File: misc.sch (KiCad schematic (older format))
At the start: 39 parts, among them J13 MICROSD_SLOT_TFP09-2-12B, P13 EXT_SD, P14 LCD, P15 LIMIT_SWITCHES, P16 LIMIT_SWITCHES_V, P17 CONN_01X03, P18 CONN_01X03, P19 CONN_01X03, P20 CONN_01X03, P21 THERMISTORS, P25 I2C, SW1 RESET, U3 ESP-12E

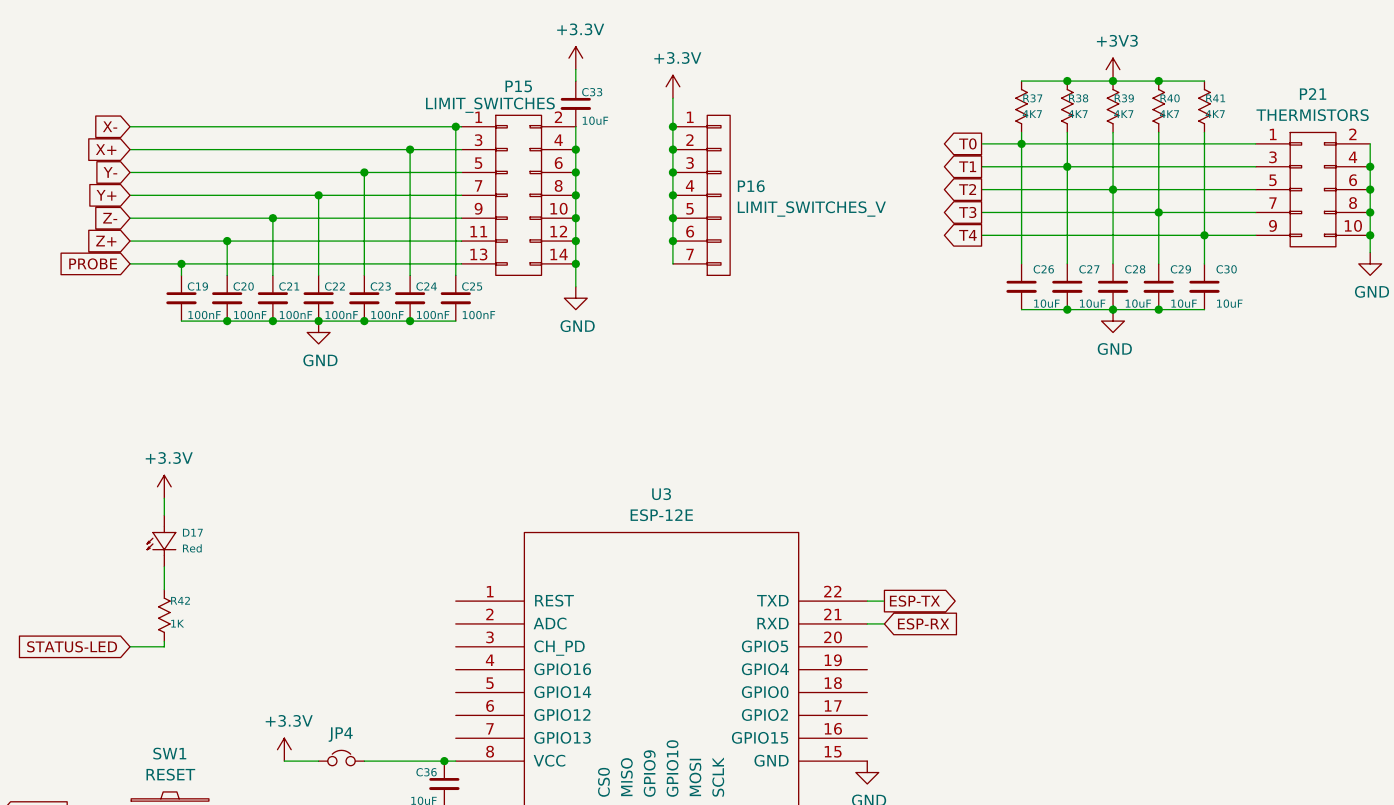
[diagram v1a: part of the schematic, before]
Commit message: Added component specifications
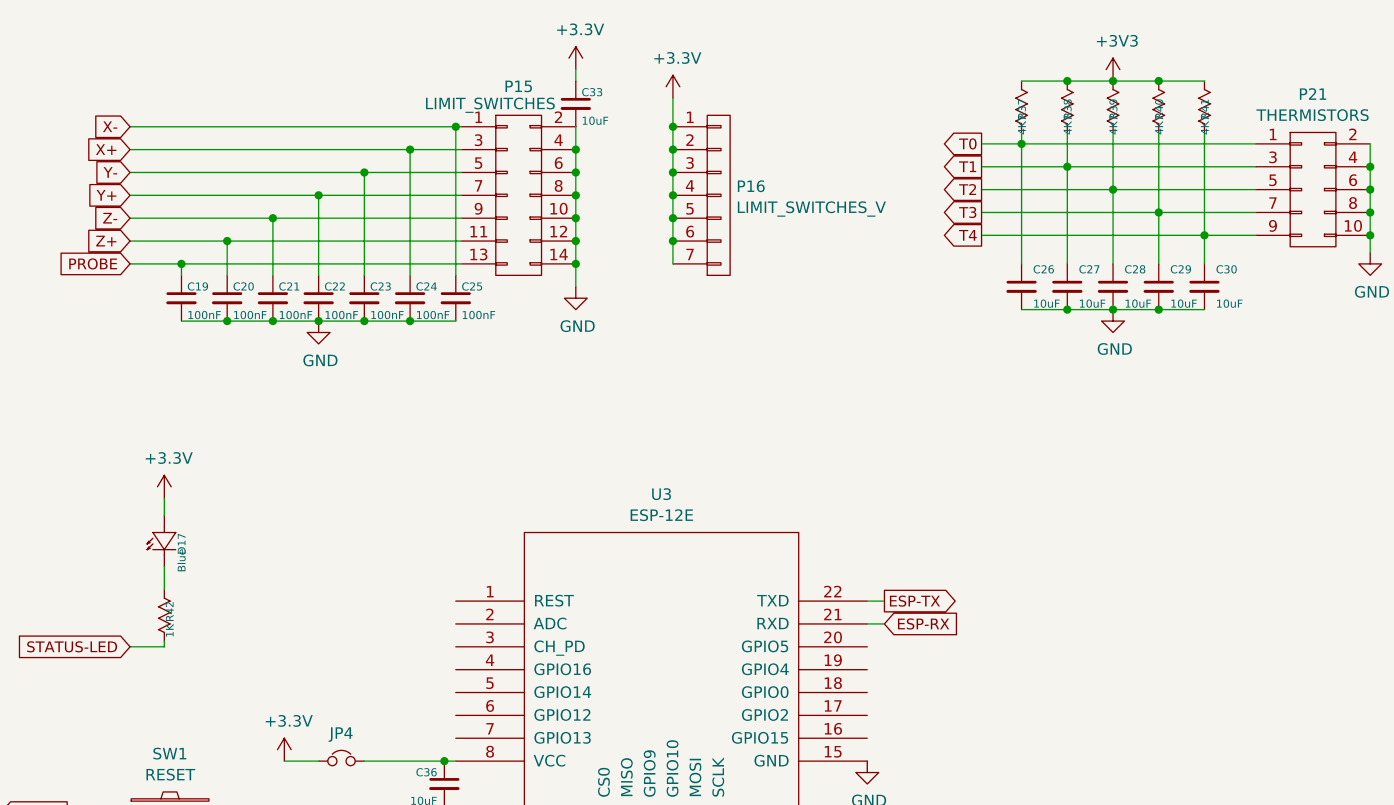
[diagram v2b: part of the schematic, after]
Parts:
- C18, C26, C27, C28, C29, C30, C33, C34, C36: Specification (none) -> X7R/X5R; VoltageRating (none) -> 6.3V
- C19, C20, C21, C22, C23, C24, C25, C31: Specification (none) -> X7R; VoltageRating (none) -> 16V
- D17: value Red -> Blue
- J13: ManufacturerNo (none) -> TFP09-2-12B
- R37, R38, R39, R40, R41: Specification (none) -> 1%
- R42: Specification (none) -> 5%
- U3: Manufacturer (none) -> AI-Thinker; ManufacturerNo (none) -> ESP-12E
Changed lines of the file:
@@
 F 2 "geda-footprints:MICROSD_SLOT_TFP09-2-12B" H 2075 2350 60  0001 C CNN
 F 3 "" H 2075 2350 60  0000 C CNN
+F 4 "TFP09-2-12B" H 2075 2350 135 0001 L CNN "ManufacturerNo"
 	1    2075 2350
 	1    0    0    -1
@@
 F 2 "capacitors:C_0805" H 1825 1875 50  0001 C CNN
 F 3 "" H 1825 1875 50  0000 C CNN
+F 4 "6.3V" H 1825 1875 135 0001 L CNN "VoltageRating"
+F 5 "X7R/X5R" H 1825 1875 135 0001 L CNN "Specification"
 	1    1825 1875
 	1    0    0    -1
@@
 U 1 1 568D8616
 P 8750 1325
-F 0 "R39" V 8827 1403 34  0000 L CNN
-F 1 "4K7" V 8896 1403 34  0000 L CNN
+F 0 "R39" H 8827 1403 34  0000 L CNN
+F 1 "4K7" H 8896 1403 34  0000 L CNN
 F 2 "resistors:R_0603" H 8750 1325 60  0001 C CNN
 F 3 "" H 8750 1325 60  0000 C CNN
+F 4 "1%" H 8750 1325 135 0001 L CNN "Specification"
 	1    8750 1325
 	0    1    1    0
@@
 F 2 "capacitors:C_0805" H 9225 2225 50  0001 C CNN
 F 3 "" H 9225 2225 50  0000 C CNN
+F 4 "6.3V" H 9225 2225 135 0001 L CNN "VoltageRating"
+F 5 "X7R/X5R" H 9225 2225 135 0001 L CNN "Specification"
 	1    9225 2225
 	1    0    0    -1
@@
 U 1 1 568D8A52
 P 9150 1325
-F 0 "R41" V 9227 1403 34  0000 L CNN
-F 1 "4K7" V 9296 1403 34  0000 L CNN
+F 0 "R41" H 9227 1403 34  0000 L CNN
+F 1 "4K7" H 9296 1403 34  0000 L CNN
 F 2 "resistors:R_0603" H 9150 1325 60  0001 C CNN
 F 3 "" H 9150 1325 60  0000 C CNN
+F 4 "1%" H 9150 1325 135 0001 L CNN "Specification"
 	1    9150 1325
 	0    1    1    0
@@
 U 1 1 568D8AA1
 P 8950 1325
-F 0 "R40" V 9027 1403 34  0000 L CNN
-F 1 "4K7" V 9096 1403 34  0000 L CNN
+F 0 "R40" H 9027 1403 34  0000 L CNN
+F 1 "4K7" H 9096 1403 34  0000 L CNN
 F 2 "resistors:R_0603" H 8950 1325 60  0001 C CNN
 F 3 "" H 8950 1325 60  0000 C CNN
+F 4 "1%" H 8950 1325 135 0001 L CNN "Specification"
 	1    8950 1325
 	0    1    1    0
@@
 U 1 1 568D8B17
 P 8550 1325
-F 0 "R38" V 8627 1403 34  0000 L CNN
-F 1 "4K7" V 8696 1403 34  0000 L CNN
+F 0 "R38" H 8627 1403 34  0000 L CNN
+F 1 "4K7" H 8696 1403 34  0000 L CNN
 F 2 "resistors:R_0603" H 8550 1325 60  0001 C CNN
 F 3 "" H 8550 1325 60  0000 C CNN
+F 4 "1%" H 8550 1325 135 0001 L CNN "Specification"
 	1    8550 1325
 	0    1    1    0
@@
 U 1 1 568D8BC2
 P 8350 1325
-F 0 "R37" V 8427 1403 34  0000 L CNN
-F 1 "4K7" V 8496 1403 34  0000 L CNN
+F 0 "R37" H 8427 1403 34  0000 L CNN
+F 1 "4K7" H 8496 1403 34  0000 L CNN
 F 2 "resistors:R_0603" H 8350 1325 60  0001 C CNN
 F 3 "" H 8350 1325 60  0000 C CNN
+F 4 "1%" H 8350 1325 135 0001 L CNN "Specification"
 	1    8350 1325
 	0    1    1    0
@@
 F 2 "capacitors:C_0805" H 9025 2225 50  0001 C CNN
 F 3 "" H 9025 2225 50  0000 C CNN
+F 4 "6.3V" H 9025 2225 135 0001 L CNN "VoltageRating"
+F 5 "X7R/X5R" H 9025 2225 135 0001 L CNN "Specification"
 	1    9025 2225
 	1    0    0    -1
@@
 F 2 "capacitors:C_0805" H 8825 2225 50  0001 C CNN
 F 3 "" H 8825 2225 50  0000 C CNN
+F 4 "6.3V" H 8825 2225 135 0001 L CNN "VoltageRating"
+F 5 "X7R/X5R" H 8825 2225 135 0001 L CNN "Specification"
 	1    8825 2225
 	1    0    0    -1
@@
 F 2 "capacitors:C_0805" H 8625 2225 50  0001 C CNN
 F 3 "" H 8625 2225 50  0000 C CNN
+F 4 "6.3V" H 8625 2225 135 0001 L CNN "VoltageRating"
+F 5 "X7R/X5R" H 8625 2225 135 0001 L CNN "Specification"
 	1    8625 2225
 	1    0    0    -1
@@
 F 2 "capacitors:C_0805" H 8425 2225 50  0001 C CNN
 F 3 "" H 8425 2225 50  0000 C CNN
+F 4 "6.3V" H 8425 2225 135 0001 L CNN "VoltageRating"
+F 5 "X7R/X5R" H 8425 2225 135 0001 L CNN "Specification"
 	1    8425 2225
 	1    0    0    -1
@@
 F 2 "capacitors:C_0603" H 5950 2275 50  0001 C CNN
 F 3 "" H 5950 2275 50  0000 C CNN
+F 4 "16V" H 5950 2275 135 0001 L CNN "VoltageRating"
+F 5 "X7R" H 5950 2275 135 0001 L CNN "Specification"
 	1    5950 2275
 	1    0    0    -1
@@
 F 2 "capacitors:C_0603" H 5750 2275 50  0001 C CNN
 F 3 "" H 5750 2275 50  0000 C CNN
+F 4 "16V" H 5750 2275 135 0001 L CNN "VoltageRating"
+F 5 "X7R" H 5750 2275 135 0001 L CNN "Specification"
 	1    5750 2275
 	1    0    0    -1
@@
 F 2 "capacitors:C_0603" H 5550 2275 50  0001 C CNN
 F 3 "" H 5550 2275 50  0000 C CNN
+F 4 "16V" H 5550 2275 135 0001 L CNN "VoltageRating"
+F 5 "X7R" H 5550 2275 135 0001 L CNN "Specification"
 	1    5550 2275
 	1    0    0    -1
@@
 F 2 "capacitors:C_0603" H 5350 2275 50  0001 C CNN
 F 3 "" H 5350 2275 50  0000 C CNN
+F 4 "16V" H 5350 2275 135 0001 L CNN "VoltageRating"
+F 5 "X7R" H 5350 2275 135 0001 L CNN "Specification"
 	1    5350 2275
 	1    0    0    -1
@@
 F 2 "capacitors:C_0603" H 5150 2275 50  0001 C CNN
 F 3 "" H 5150 2275 50  0000 C CNN
+F 4 "16V" H 5150 2275 135 0001 L CNN "VoltageRating"
+F 5 "X7R" H 5150 2275 135 0001 L CNN "Specification"
 	1    5150 2275
 	1    0    0    -1
@@
 F 2 "capacitors:C_0603" H 4950 2275 50  0001 C CNN
 F 3 "" H 4950 2275 50  0000 C CNN
+F 4 "16V" H 4950 2275 135 0001 L CNN "VoltageRating"
+F 5 "X7R" H 4950 2275 135 0001 L CNN "Specification"
 	1    4950 2275
 	1    0    0    -1
@@
 F 2 "capacitors:C_0603" H 4750 2275 50  0001 C CNN
 F 3 "" H 4750 2275 50  0000 C CNN
+F 4 "16V" H 4750 2275 135 0001 L CNN "VoltageRating"
+F 5 "X7R" H 4750 2275 135 0001 L CNN "Specification"
 	1    4750 2275
 	1    0    0    -1
@@
 U 1 1 568F7EEA
 P 4725 3450
-F 0 "D17" V 4873 3423 34  0000 R CNN
-F 1 "Red" V 4804 3423 34  0000 R CNN
+F 0 "D17" H 4873 3423 34  0000 R CNN
+F 1 "Blue" H 4804 3423 34  0000 R CNN
 F 2 "diodes:LED-0603" H 4725 3450 60  0001 C CNN
 F 3 "" H 4725 3450 60  0000 C CNN
@@
 U 1 1 568F903C
 P 4600 3550
-F 0 "R42" V 4650 3650 34  0000 L CNN
-F 1 "1K" V 4750 3650 34  0000 L CNN
+F 0 "R42" H 4650 3650 34  0000 L CNN
+F 1 "1K" H 4750 3650 34  0000 L CNN
 F 2 "resistors:R_0603" H 4600 3550 60  0001 C CNN
 F 3 "" H 4600 3550 60  0000 C CNN
+F 4 "5%" H 4600 3550 135 0001 L CNN "Specification"
 	1    4600 3550
 	0    1    1    0
@@
 F 2 "capacitors:C_0603" H 4375 4700 50  0001 C CNN
 F 3 "" H 4375 4700 50  0000 C CNN
+F 4 "16V" H 4375 4700 135 0001 L CNN "VoltageRating"
+F 5 "X7R" H 4375 4700 135 0001 L CNN "Specification"
 	1    4375 4700
 	1    0    0    -1
@@
 F 2 "capacitors:C_0805" H 6475 1425 50  0001 C CNN
 F 3 "" H 6475 1425 50  0000 C CNN
+F 4 "6.3V" H 6475 1425 135 0001 L CNN "VoltageRating"
+F 5 "X7R/X5R" H 6475 1425 135 0001 L CNN "Specification"
 	1    6475 1425
 	1    0    0    -1
@@
 F 2 "capacitors:C_0805" H 2775 6625 50  0001 C CNN
 F 3 "" H 2775 6625 50  0000 C CNN
+F 4 "6.3V" H 2775 6625 135 0001 L CNN "VoltageRating"
+F 5 "X7R/X5R" H 2775 6625 135 0001 L CNN "Specification"
 	1    2775 6625
 	1    0    0    -1
@@
 F 2 "misc:ESP-12E" H 6850 3900 50  0001 C CNN
 F 3 "" H 6850 3900 50  0001 C CNN
+F 4 "AI-Thinker" H 6850 3900 135 0001 L CNN "Manufacturer"
+F 5 "ESP-12E" H 6850 3900 135 0001 L CNN "ManufacturerNo"
 	1    6850 3900
 	1    0    0    -1
@@
 F 2 "capacitors:C_0805" H 5900 4400 50  0001 C CNN
 F 3 "" H 5900 4400 50  0000 C CNN
+F 4 "6.3V" H 5900 4400 135 0001 L CNN "VoltageRating"
+F 5 "X7R/X5R" H 5900 4400 135 0001 L CNN "Specification"
 	1    5900 4400
 	1    0    0    -1
